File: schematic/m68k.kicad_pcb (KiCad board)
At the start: 2 copper layers, 45 parts, among them J1 Power, J2 CONN_01X03, J3 JTAG, J4 CONN_02X30, J5 I2C, J6 CONN_02X30, J7 CONN_01X02, J8 CONN_02X30, J9 CONN_01X03, SW1 SW_Push_Dual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

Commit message: layout work
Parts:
- moved R15 50.0 mm to (132.9, 52.3)
- moved R16 50.0 mm to (132.9, 54.8)
- moved J5 50.0 mm to (125.3, 57.4)
- moved U4 33.7 mm to (151.8, 72.2), turned to 90 degrees
- moved C15 30.1 mm to (90.4, 75.6), turned to 90 degrees
- moved C8 27.0 mm to (148.3, 84.8), turned to 270 degrees
- moved C14 24.3 mm to (52.1, 57.6)
- moved R14 24.3 mm to (52.4, 63.2)
- moved U9 24.3 mm to (65.1, 60.7)
- moved C13 23.4 mm to (53.6, 70.7)
- moved R13 23.4 mm to (53.6, 75.8)
- moved U8 23.4 mm to (65.1, 71.9)
- moved C10 19.9 mm to (93.0, 131.5)
- moved C11 19.9 mm to (84.1, 116.2)
- moved R2 19.9 mm to (93.0, 125.1)
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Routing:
- net /A6: track 0.00 -> 107.3 mm, vias 0 -> 2
- net /A9: track 0.00 -> 78.3 mm, vias 0 -> 2
- net /A2: track 0.00 -> 76.5 mm, vias 0 -> 2
- net /A1: track 0.00 -> 76.4 mm, vias 0 -> 2
- net /A3: track 0.00 -> 76.2 mm, vias 0 -> 2
- net /A11: track 0.00 -> 75.3 mm, vias 0 -> 4
- net /A10: track 0.00 -> 75.2 mm, vias 0 -> 2
- net /A4: track 0.00 -> 74.3 mm, vias 0 -> 2
- net /A5: track 0.00 -> 73.8 mm, vias 0 -> 2
- net /A7: track 0.00 -> 72.0 mm, vias 0 -> 2
- net /A8: track 0.00 -> 68.9 mm, vias 0 -> 2
- net /A12: track 0.00 -> 68.6 mm, vias 0 -> 2
- net /D15: track 61.3 -> 8.05 mm, vias 0 -> 1
- net /A14: track 0.00 -> 48.8 mm, vias 0 -> 2
- net /A13: track 0.00 -> 44.6 mm, vias 0 -> 2
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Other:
- board outline added: 160 x 100 mm

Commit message: - further layout
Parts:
- moved U10 77.6 mm to (71.2, 131.2), turned to 0 degrees
- moved C16 68.4 mm to (76.1, 121.2), turned to 270 degrees
- moved C15 12.4 mm to (83.7, 65.3), turned to 0 degrees
- moved C8 8.92 mm to (139.4, 84.1)
- moved C9 8.92 mm to (140.5, 114.6)
- moved U4 8.92 mm to (142.9, 71.5)
- moved U5 8.92 mm to (142.5, 102.9)
- moved C4 8.18 mm to (103.6, 89.3)
- moved C12 7.66 mm to (85.4, 141.1)
- moved C10 7.66 mm to (100.6, 132.2)
- moved C11 7.66 mm to (91.7, 117.0)
- moved R2 7.66 mm to (100.6, 125.9)
- moved U6 7.66 mm to (89.7, 128.2)
- moved C3 7.00 mm to (127.9, 90.2)
- moved U2 7.00 mm to (111.4, 81.3)
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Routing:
- net /D0: track 13.3 -> 80.6 mm, vias 1 -> 5
- net /D15: track 8.05 -> 74.6 mm, vias 1 -> 6
- net /D13: track 10.6 -> 75.3 mm, vias 1 -> 6
- net /D1: track 14.4 -> 78.2 mm, vias 1 -> 5
- net /D14: track 9.18 -> 72.7 mm, vias 1 -> 6
- net /D12: track 12.1 -> 72.5 mm, vias 1 -> 6
- net /D11: track 14.7 -> 75.0 mm, vias 1 -> 5
- net /D2: track 15.6 -> 75.7 mm, vias 1 -> 5
- net /D10: track 16.2 -> 74.5 mm, vias 1 -> 6
- net /D9: track 17.3 -> 74.0 mm, vias 1 -> 6
- net /D3: track 16.7 -> 72.9 mm, vias 1 -> 5
- net /D4: track 20.3 -> 72.0 mm, vias 1 -> 5
- net /D5: track 21.7 -> 68.3 mm, vias 1 -> 5
- net /D6: track 23.1 -> 66.4 mm, vias 1 -> 6
- net /D8: track 18.8 -> 59.9 mm, vias 1 -> 4
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
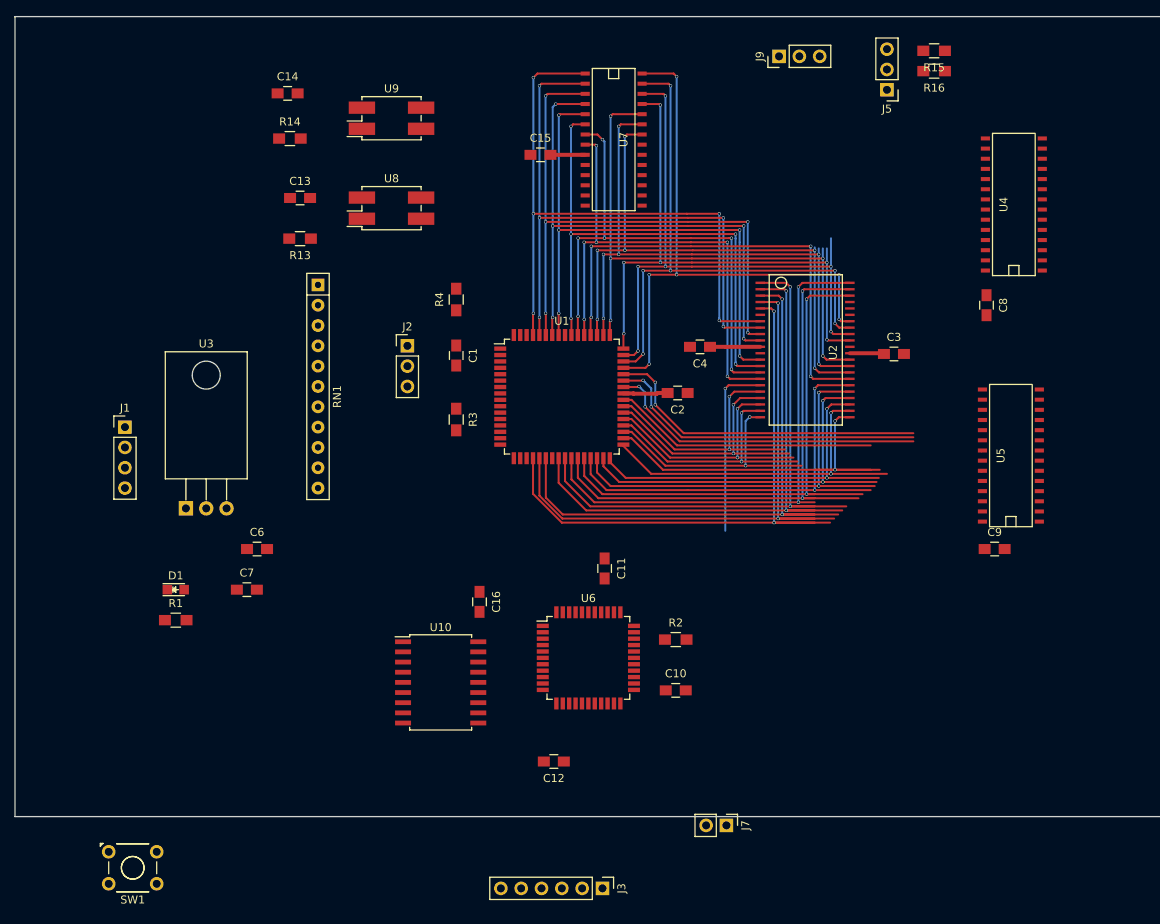
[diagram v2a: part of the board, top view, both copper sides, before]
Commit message: - changed pin assignment - further layout
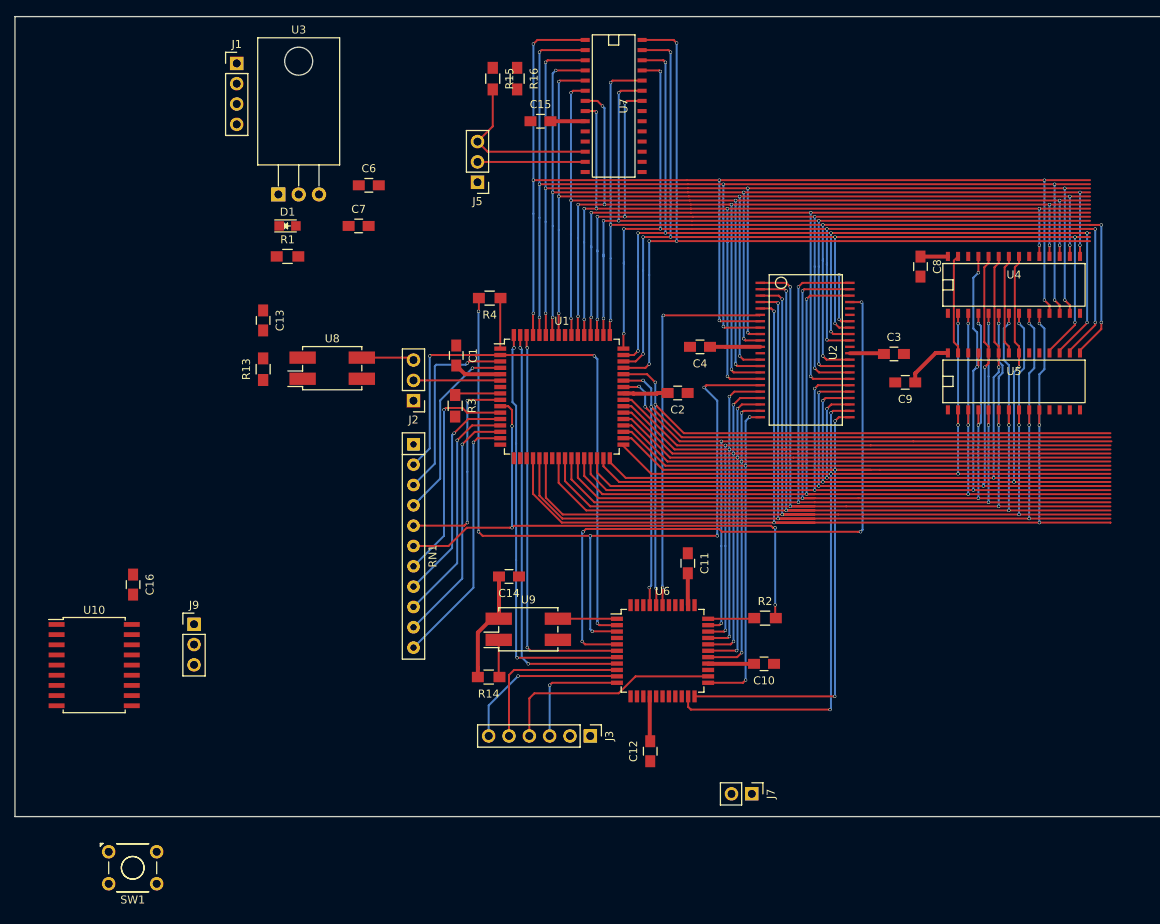
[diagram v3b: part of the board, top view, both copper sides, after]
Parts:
- moved J9 101.9 mm to (40.4, 124.0), turned to 0 degrees
- moved R14 71.8 mm to (77.2, 130.6), turned to 180 degrees
- moved C14 66.4 mm to (79.8, 118.0), turned to 180 degrees
- moved U9 66.1 mm to (82.2, 124.6)
- moved R15 55.3 mm to (77.7, 55.8), turned to 270 degrees
- moved J5 52.5 mm to (75.8, 68.7)
- moved R16 52.1 mm to (80.8, 55.8), turned to 270 degrees
- moved C6 47.6 mm to (62.2, 69.1)
- moved R1 47.6 mm to (52.1, 78.0)
- moved C7 47.6 mm to (61.0, 74.2)
- moved D1 47.6 mm to (52.1, 74.2)
- moved J1 47.6 mm to (45.7, 53.8)
- moved C16 43.4 mm to (32.8, 119.0)
- moved U10 43.4 mm to (27.9, 129.1)
- moved U3 40.9 mm to (50.9, 70.2)
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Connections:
- J4 pad 28: /D0 -> /D15
- J4 pad 29: /D1 -> /D14
- J4 pad 30: /D2 -> /D13
- J4 pad 31: /D3 -> /D12
- J4 pad 32: /D4 -> /D11
- J4 pad 33: /D5 -> /D10
- J4 pad 34: /D6 -> /D9
- J4 pad 35: /D7 -> /D8
- J4 pad 36: /D8 -> /D7
- J4 pad 37: /D9 -> /D6
- J4 pad 38: /D10 -> /D5
- J4 pad 39: /D11 -> /D4
- J4 pad 40: /D12 -> /D3
- J4 pad 41: /D13 -> /D2
- J4 pad 42: /D14 -> /D1
- J4 pad 43: /D15 -> /D0
- J6 pad 28: /D0 -> /D15
- J6 pad 29: /D1 -> /D14
- J6 pad 30: /D2 -> /D13
- J6 pad 31: /D3 -> /D12
- J6 pad 32: /D4 -> /D11
- J6 pad 33: /D5 -> /D10
- J6 pad 34: /D6 -> /D9
- J6 pad 35: /D7 -> /D8
- J6 pad 36: /D8 -> /D7
- J6 pad 37: /D9 -> /D6
- J6 pad 38: /D10 -> /D5
- J6 pad 39: /D11 -> /D4
- J6 pad 40: /D12 -> /D3
- J6 pad 41: /D13 -> /D2
- J6 pad 42: /D14 -> /D1
- J6 pad 43: /D15 -> /D0
- J8 pad 28: /D0 -> /D15
- J8 pad 29: /D1 -> /D14
- J8 pad 30: /D2 -> /D13
- J8 pad 31: /D3 -> /D12
- J8 pad 32: /D4 -> /D11
- J8 pad 33: /D5 -> /D10
- J8 pad 34: /D6 -> /D9
- J8 pad 35: /D7 -> /D8
- J8 pad 36: /D8 -> /D7
- J8 pad 37: /D9 -> /D6
- J8 pad 38: /D10 -> /D5
- J8 pad 39: /D11 -> /D4
- J8 pad 40: /D12 -> /D3
- J8 pad 41: /D13 -> /D2
- J8 pad 42: /D14 -> /D1
- J8 pad 43: /D15 -> /D0
- U6 pad 12: /~BERR -> /CS0
- U6 pad 13: /~RAM_CE -> /CS1
- U6 pad 14: /~EEPROM_LDS -> /CS2
- U6 pad 16: /~EEPROM_UDS -> /CS3
- U6 pad 37: /A22 -> /~EEPROM_LDS
- U6 pad 38: /A23 -> /~EEPROM_UDS
- U6 pad 39: /CS0 -> /~RAM_CE
- U6 pad 40: /CS1 -> /A23
- U6 pad 41: /CS2 -> /A22
- U6 pad 42: /CS3 -> /~BERR
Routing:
- net /A13: track 44.6 -> 143.3 mm, vias 2 -> 6
- net /~OE: track 0.00 -> 95.9 mm, vias 0 -> 4
- net /R/~W: track 22.3 -> 113.4 mm, vias 1 -> 6
- net /A14: track 48.8 -> 123.5 mm, vias 2 -> 3
- net /~RESET: track 0.00 -> 74.1 mm, vias 0 -> 4
- net /D0: track 80.6 -> 152.3 mm, vias 5 -> 7
- net /~DTACK: track 0.00 -> 71.2 mm, vias 0 -> 3
- net /D1: track 78.2 -> 148.9 mm, vias 5 -> 7
- net /A15: track 31.7 -> 101.9 mm, vias 2 -> 3
- net /A16: track 32.2 -> 99.6 mm, vias 2 -> 3
- net /A17: track 32.6 -> 100.0 mm, vias 2 -> 3
- net /D2: track 75.7 -> 143.1 mm, vias 5 -> 7
- net /A19: track 33.2 -> 100.2 mm, vias 2 -> 3
- net /A18: track 32.7 -> 99.6 mm, vias 2 -> 3
- net /A1: track 76.4 -> 140.1 mm, vias 2 -> 5
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
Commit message: further layout
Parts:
- moved SW1 93.4 mm to (121.4, 134.5)
- moved C16 81.3 mm to (114.0, 116.8)
- moved J9 81.3 mm to (121.7, 121.8)
- moved U10 81.3 mm to (109.2, 126.9)
- moved J6 60.1 mm to (163.6, 133.6)
- moved J4 60.1 mm to (215.6, 133.6)
- moved J8 60.1 mm to (189.0, 133.6)
- moved C11 24.6 mm to (77.5, 116.2)
- moved C12 24.6 mm to (72.8, 139.7)
- moved C4 24.6 mm to (79.0, 89.2)
- moved C8 24.6 mm to (106.6, 79.1)
- moved C9 24.6 mm to (104.6, 93.6)
- moved J5 24.6 mm to (51.2, 68.6)
- moved R15 24.6 mm to (53.1, 55.6)
- moved R16 24.6 mm to (56.1, 55.6)
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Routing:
- net /CS1: track 0.00 -> 98.8 mm, vias 0 -> 4
- net /CLK_FROM_CPLD: track 0.00 -> 89.2 mm, vias 0 -> 2
- net /CS0: track 0.00 -> 87.9 mm, vias 0 -> 4
- net /~EEPROM_LDS: track 0.00 -> 86.4 mm, vias 0 -> 2
- net /CS2: track 0.00 -> 85.9 mm, vias 0 -> 4
- net /CS3: track 0.00 -> 84.1 mm, vias 0 -> 4
- net /~EEPROM_UDS: track 0.00 -> 75.8 mm, vias 0 -> 2
- net /CLK_16MHz: track 6.59 -> 68.0 mm, vias 0 -> 1
- net /R/~W: track 113.4 -> 170.6 mm, vias 6 -> 10
- net /~BERR: track 27.8 -> 58.8 mm, vias 1 -> 4
- net /~OE: track 95.9 -> 113.7 mm, vias 4 -> 7
- net /A12: track 104.5 -> 106.8 mm, vias 4 -> 5
- net /A11: track 109.1 -> 110.8 mm, vias 4 -> 5
- net /A10: track 111.7 -> 113.2 mm, vias 4 -> 5
- net /A4: track 134.9 -> 134.4 mm

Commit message: layout pretty far
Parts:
- moved D1 135.3 mm to (159.2, 43.3), turned to 270 degrees
- moved R1 133.0 mm to (155.9, 43.4), turned to 270 degrees
- moved U3 103.1 mm to (125.4, 41.7), turned to 270 degrees
- moved C7 82.8 mm to (115.6, 50.1), turned to 180 degrees
- moved C6 81.1 mm to (115.6, 46.8), turned to 180 degrees
- moved R13 76.9 mm to (94.9, 61.4), turned to 180 degrees
- moved C13 73.3 mm to (94.8, 65.4), turned to 180 degrees
- moved U8 59.5 mm to (85.0, 62.8), turned to 180 degrees
- moved J1 56.9 mm to (76.6, 41.6)
- moved J7 45.2 mm to (126.5, 126.2)
- moved SW1 40.7 mm to (156.5, 113.9), turned to 90 degrees
- moved J5 37.9 mm to (86.5, 54.8)
- moved C3 36.3 mm to (136.7, 76.0)
- moved R2 36.3 mm to (120.6, 109.0)
- moved R4 36.3 mm to (86.2, 69.0)
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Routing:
- net +3V3: track 65.7 -> 581.6 mm, vias 0 -> 11
- net /~IPL0: track 32.3 -> 303.9 mm, vias 1 -> 6
- net +5V: track 0.00 -> 264.7 mm, vias 0 -> 1
- net /~IPL1: track 30.8 -> 289.9 mm, vias 1 -> 5
- net /~IPL2: track 29.2 -> 286.1 mm, vias 1 -> 5
- net /~BR: track 23.7 -> 277.2 mm, vias 1 -> 5
- net /~BG: track 24.4 -> 277.0 mm, vias 1 -> 5
- net /~AVEC: track 28.5 -> 277.7 mm, vias 1 -> 5
- net /SDA: track 13.5 -> 201.6 mm, vias 0 -> 5
- net /SCL: track 21.3 -> 201.9 mm, vias 0 -> 5
- net /~LDS: track 53.2 -> 208.0 mm, vias 2 -> 4
- net /~DTACK: track 71.2 -> 212.6 mm, vias 3 -> 4
- net /D8: track 103.3 -> 231.7 mm, vias 4 -> 8
- net /~HALT: track 26.3 -> 150.1 mm, vias 2 -> 9
- net /R/~W: track 170.6 -> 292.3 mm, vias 10 -> 13
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- added copper zone on B.Cu, net GND
- added copper zone on F.Cu, net GND
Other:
- board size 160 x 100 mm -> 167 x 100 mm

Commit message: further layout
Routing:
- net /~UDS: track 164.0 -> 209.1 mm, vias 2 -> 4
- net /A1: track 182.9 -> 209.5 mm
- net /D8: track 231.7 -> 236.6 mm
- net /A2: track 210.0 -> 205.4 mm
- net /A3: track 211.7 -> 207.6 mm
- net /D12: track 204.6 -> 208.5 mm
- net /D5: track 210.6 -> 214.4 mm
- net /A4: track 204.8 -> 201.2 mm
- net /D15: track 199.8 -> 203.3 mm
- net /D9: track 230.8 -> 234.2 mm
- net /D13: track 203.8 -> 207.1 mm
- net /A5: track 206.2 -> 203.1 mm
- net /D4: track 216.6 -> 219.1 mm
- net /D10: track 236.1 -> 238.0 mm
- net /D14: track 208.5 -> 206.6 mm
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
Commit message: layout done
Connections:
- J4 pad 54: /BOOT -> Net-(J4-Pad54)
- J6 pad 54: /BOOT -> Net-(J6-Pad54)
- J8 pad 54: /BOOT -> Net-(J8-Pad54)
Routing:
- net GND: track 0.00 -> 62.5 mm, vias 0 -> 182
- net /BOOT: track 96.4 -> 43.8 mm
- net +5V: track 264.7 -> 270.0 mm
- net (no net): vias 0 -> 8

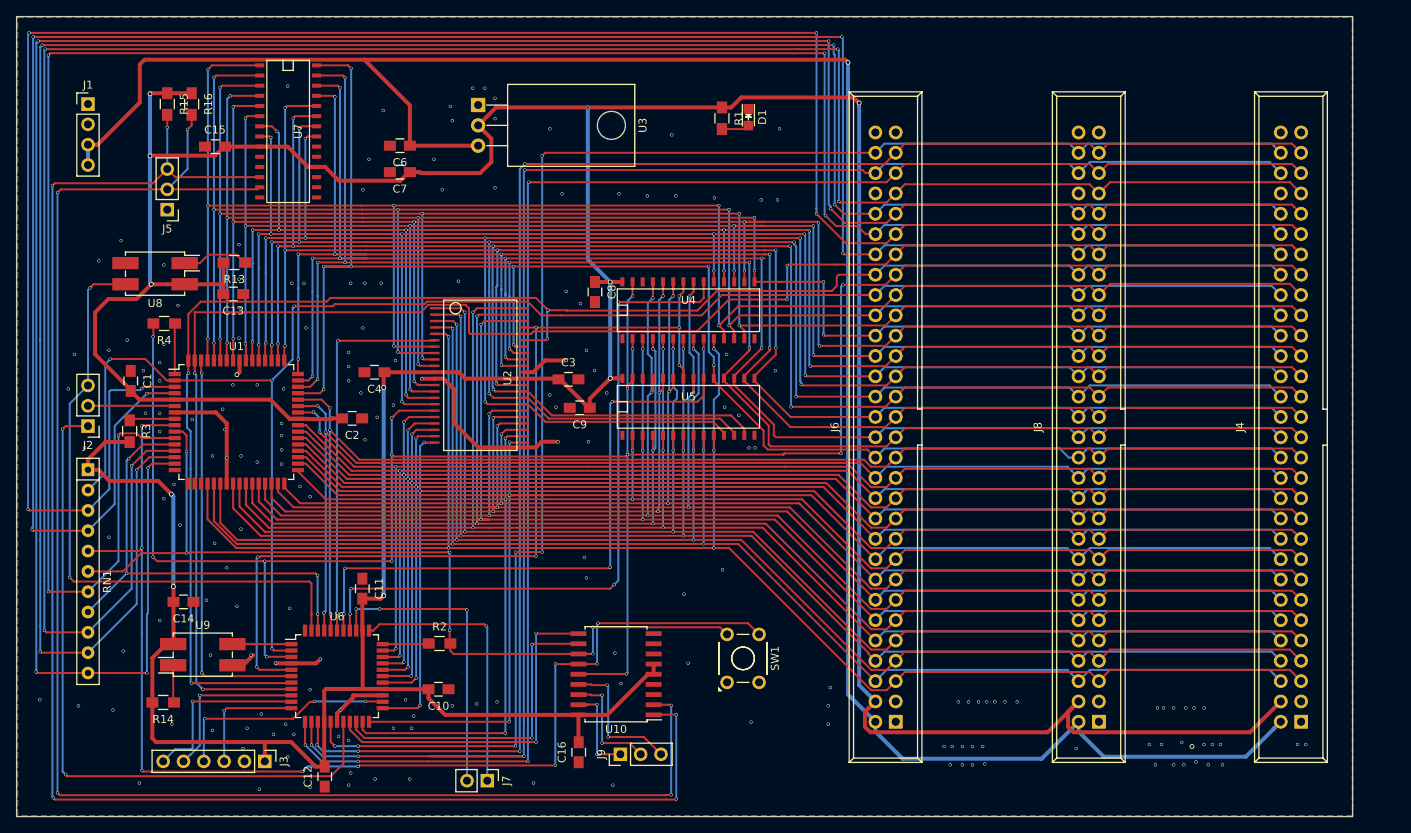
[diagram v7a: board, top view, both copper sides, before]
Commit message: new design rules and fresh layout
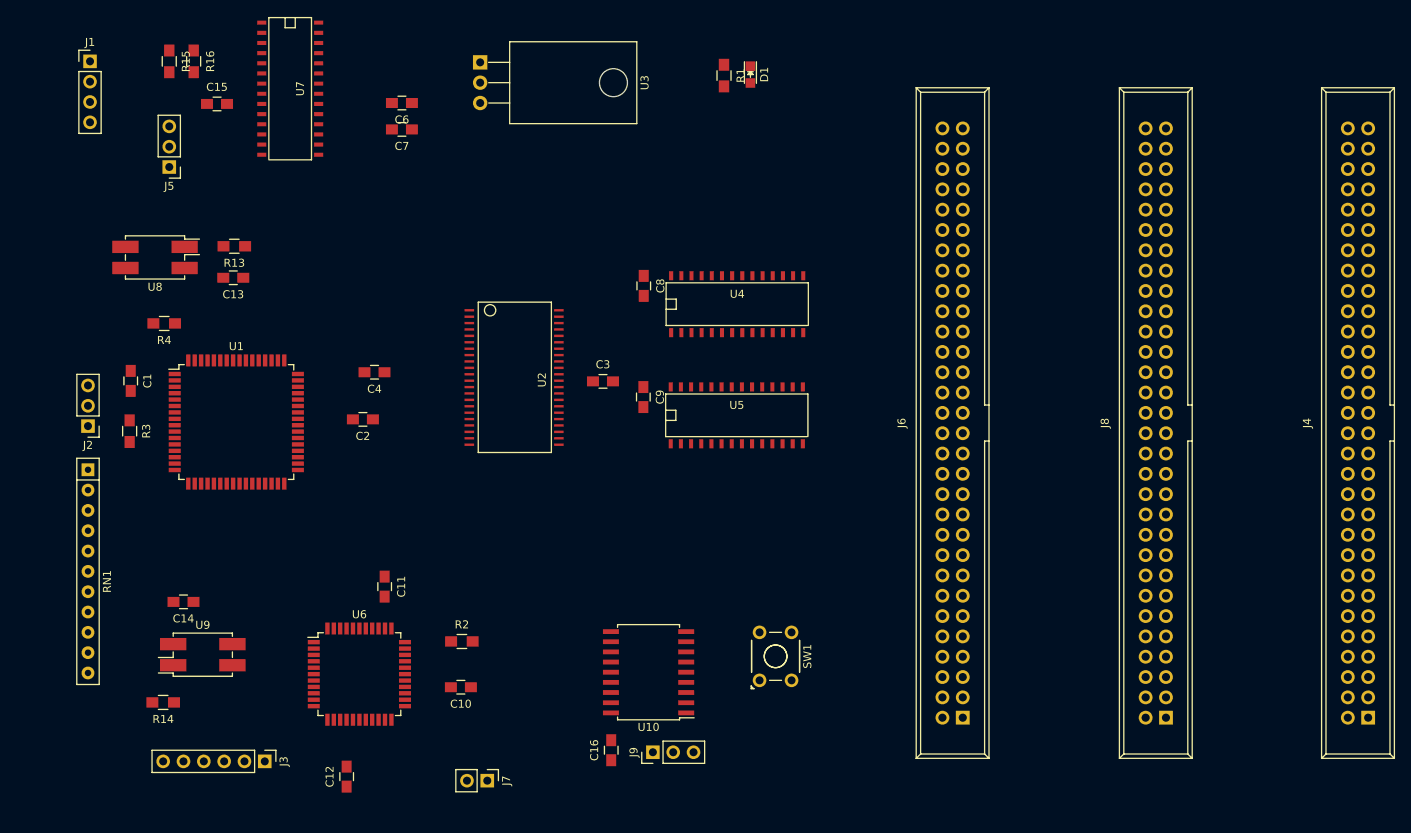
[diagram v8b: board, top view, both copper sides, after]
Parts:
- moved J4 8.40 mm to (236.7, 118.3)
- moved J6 8.40 mm to (186.0, 118.3)
- moved J8 8.40 mm to (211.4, 118.3)
- moved C9 8.06 mm to (146.1, 78.2), turned to 270 degrees
- moved C8 6.14 mm to (146.1, 64.3)
- moved U4 6.14 mm to (157.8, 66.6)
- moved U5 6.14 mm to (157.7, 80.5)
- moved J1 5.34 mm to (76.9, 36.3)
- moved R1 5.34 mm to (156.1, 38.0)
- moved D1 5.34 mm to (159.4, 37.9)
- moved J5 5.34 mm to (86.8, 49.5)
- moved R15 5.34 mm to (86.8, 36.3)
- moved R16 5.34 mm to (89.8, 36.3)
- moved C15 5.34 mm to (92.8, 41.6)
- moved U3 5.34 mm to (125.7, 36.4)
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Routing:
- net +3V3: track 581.6 -> 0.00 mm, vias 11 -> 0
- net /~IPL0: track 303.9 -> 0.00 mm, vias 6 -> 0
- net /R/~W: track 292.5 -> 0.00 mm, vias 13 -> 0
- net /~IPL1: track 289.9 -> 0.00 mm, vias 5 -> 0
- net /~IPL2: track 286.1 -> 0.00 mm, vias 5 -> 0
- net /~AVEC: track 277.7 -> 0.00 mm, vias 5 -> 0
- net /~BR: track 277.2 -> 0.00 mm, vias 5 -> 0
- net /~BG: track 277.0 -> 0.00 mm, vias 5 -> 0
- net +5V: track 270.0 -> 0.00 mm, vias 1 -> 0
- net /D10: track 238.0 -> 0.00 mm, vias 8 -> 0
- net /D8: track 236.6 -> 0.00 mm, vias 8 -> 0
- net /D9: track 234.2 -> 0.00 mm, vias 8 -> 0
- net /D0: track 223.0 -> 0.00 mm, vias 7 -> 0
- net /D4: track 219.1 -> 0.00 mm, vias 9 -> 0
- net /D1: track 215.8 -> 0.00 mm, vias 7 -> 0
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- removed copper zone on B.Cu, net GND
- removed copper zone on F.Cu, net GND
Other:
- board outline removed
- net class Default: via_dia 0.4 -> 0.6
- net class Power: via_dia 0.6 -> 0.7
- rule via_min_size: 0.4 -> 0.6
